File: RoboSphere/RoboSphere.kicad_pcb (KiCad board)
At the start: 2 copper layers, 2 parts, among them U1 RASPBERRY_PI_ZERO_2_W, U4 DRV8833PW

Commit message: Kicad H-bridge update
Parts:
- added C1: 0.01uF, Capacitor_SMD:C_0805_2012Metric, F.Cu at (41.0, 56.3)
- added C2: 10uF, Capacitor_SMD:C_0805_2012Metric, F.Cu at (41.0, 59.3)
- added C3: 2.2uF, Capacitor_SMD:C_0805_2012Metric, F.Cu at (41.0, 62.3)
- added J2: Conn_01x04_Pin, Connector_PinHeader_2.54mm:PinHeader_1x04_P2.54mm_Vertical, F.Cu at (27.3, 57.1)
- moved U1 4.97 mm to (60.0, 38.5)
- moved U4 2.36 mm to (34.4, 58.1)
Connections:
- U4 pad 10: Net-(U4-BIN2) -> Net-(U1-GPIO2/SDA1)
- U4 pad 12: Net-(U4-VM) -> +10V
- U4 pad 13: Net-(U4-GND) -> GND
- U4 pad 14: unconnected-(U4-VINT-Pad14) -> Net-(U4-VINT)
- U4 pad 15: Net-(U4-AIN2) -> Net-(U1-GPIO4/GPIO_GCLK)
- U4 pad 16: Net-(U4-AIN1) -> Net-(U1-GPIO5)
- U4 pad 2: Net-(M4-+) -> /AOUT1
- U4 pad 4: Net-(M4--) -> /AOUT2
- U4 pad 5: Net-(M1-+) -> /BOUT2
- U4 pad 7: Net-(M1--) -> /BOUT1
- U4 pad 9: Net-(U4-BIN1) -> Net-(U1-GPIO3/SCL)

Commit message: Power Converter Module
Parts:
- removed J2: Conn_01x04_Pin, Connector_PinHeader_2.54mm:PinHeader_1x04_P2.54mm_Vertical
- removed U4: DRV8833PW, Package_SO:TSSOP-16_4.4x5mm_P0.65mm
- added 3350mAh1: 3.6V, Battery:BatteryHolder_Keystone_1042_1x18650, F.Cu at (67.6, 101.0)
- added 3350mAh2: 3.6V, Battery:BatteryHolder_Keystone_1042_1x18650, F.Cu at (67.6, 78.3)
- added AOUT1: Conn_01x03_Pin, Connector_PinHeader_2.54mm:PinHeader_1x03_P2.54mm_Vertical_SMD_Pin1Left, F.Cu at (44.3, 44.5)
- added AOUT2: Conn_01x03_Pin, Connector_PinHeader_2.54mm:PinHeader_1x03_P2.54mm_Vertical_SMD_Pin1Left, F.Cu at (29.8, 44.5)
- added BOUT1: Conn_01x03_Pin, Connector_PinHeader_2.54mm:PinHeader_1x03_P2.54mm_Vertical_SMD_Pin1Left, F.Cu at (44.3, 56.5)
- added BOUT2: Conn_01x03_Pin, Connector_PinHeader_2.54mm:PinHeader_1x03_P2.54mm_Vertical_SMD_Pin1Left, F.Cu at (29.8, 56.5)
- added U2: DRV8833PWP, Package_SO:HTSSOP-16-1EP_4.4x5mm_P0.65mm_EP3.4x5mm_Mask2.46x2.31mm_ThermalVias, F.Cu at (55.4, 50.5)
- moved U1 74.6 mm to (134.5, 35.0)
- moved C3 28.3 mm to (64.3, 46.3)
- moved C2 25.9 mm to (65.2, 50.2), turned to 90 degrees
- moved C1 23.3 mm to (64.2, 54.3), turned to 180 degrees
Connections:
- net +10V renamed +6V
- U1 pad 33: unconnected-(U1-GPIO13-Pad33) -> Net-(U1-GPIO13)
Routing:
- net GND: track 0.00 -> 60.6 mm
- net /AOUT2: track 0.00 -> 39.2 mm
- net /BOUT2: track 0.00 -> 38.8 mm
- net /AOUT1: track 0.00 -> 24.1 mm
- net /BOUT1: track 0.00 -> 23.8 mm
- net +6V: track 0.00 -> 10.3 mm
- net Net-(U2-VINT): track 0.00 -> 6.45 mm
- net Net-(U2-VCP): track 0.00 -> 6.16 mm
- net +5V: track 0.00 -> 2.54 mm

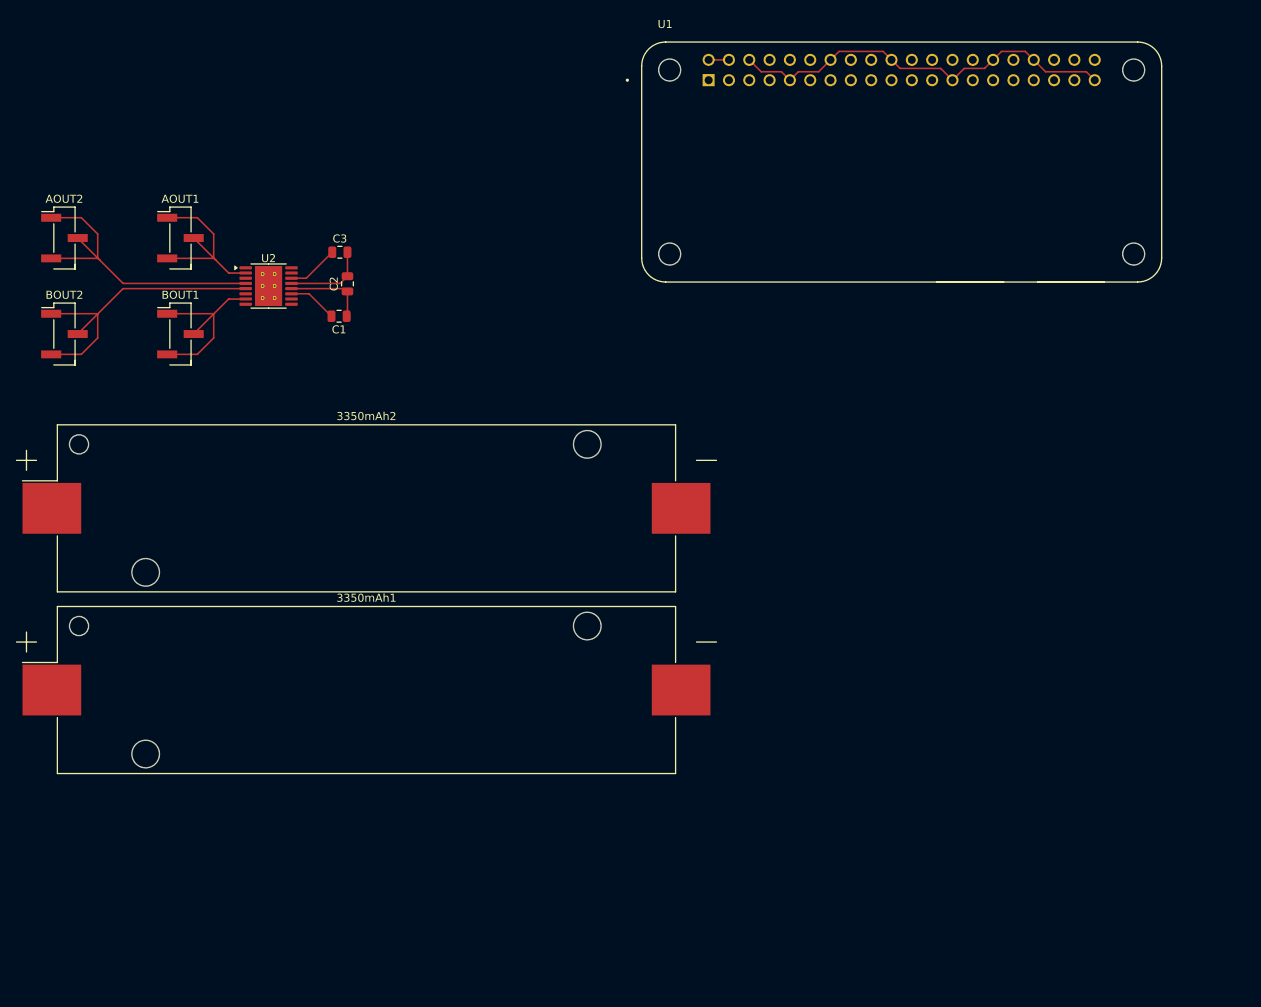
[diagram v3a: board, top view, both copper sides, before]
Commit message: Updated schematic with placement organization
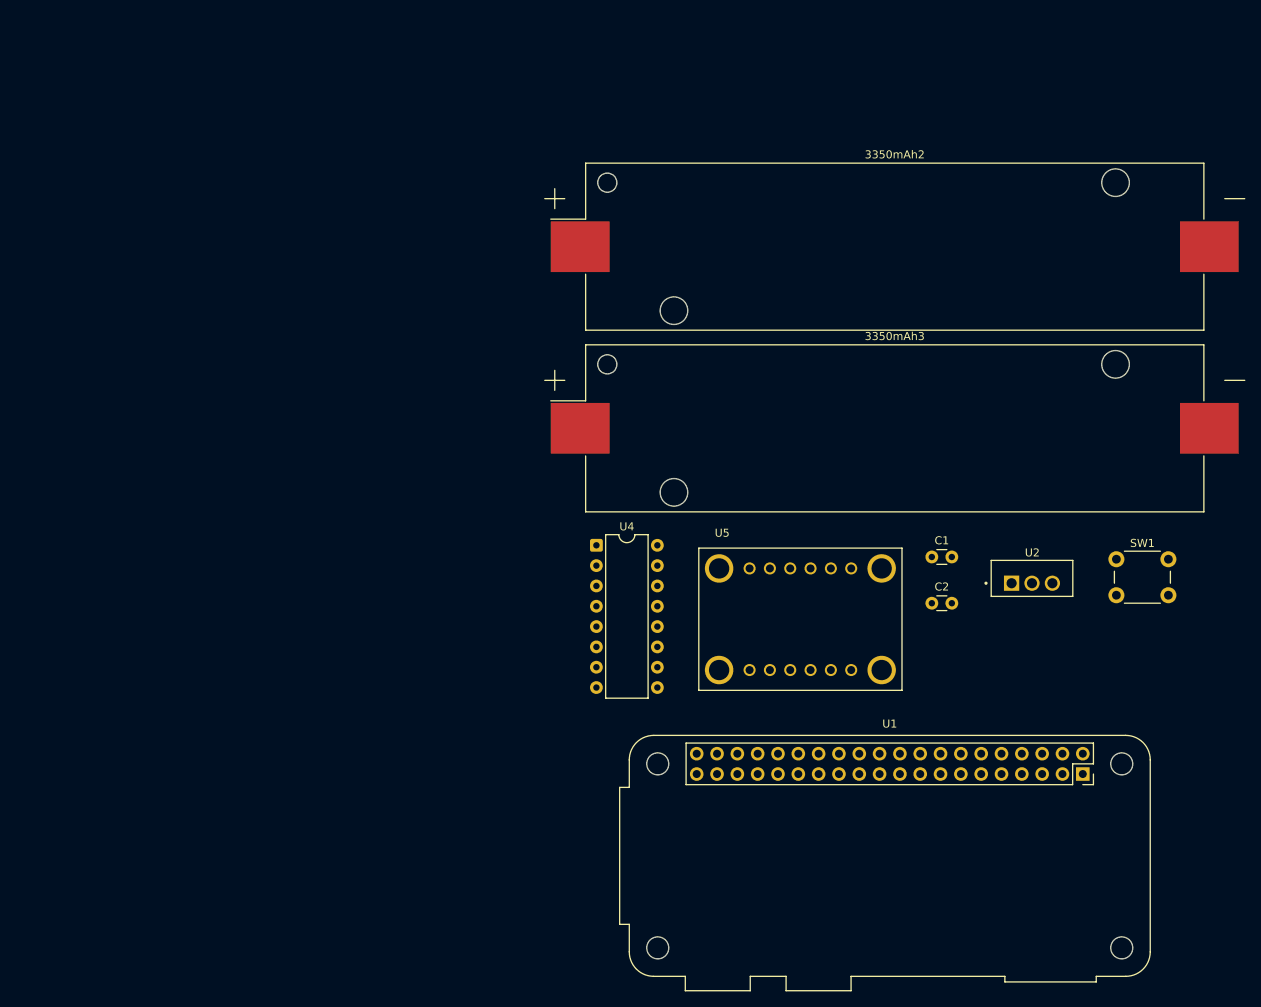
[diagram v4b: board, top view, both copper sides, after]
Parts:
- removed 3350mAh1: 3.6V, Battery:BatteryHolder_Keystone_1042_1x18650
- removed AOUT1, AOUT2, BOUT1, BOUT2: Conn_01x03_Pin, Connector_PinHeader_2.54mm:PinHeader_1x03_P2.54mm_Vertical_SMD_Pin1Left
- removed C3: 2.2uF, Capacitor_SMD:C_0805_2012Metric
- added 3350mAh3: 3.7V, Battery:BatteryHolder_Keystone_1042_1x18650, F.Cu at (133.6, 68.3)
- added SW1: SW_Push, Button_Switch_THT:SW_PUSH_6mm, F.Cu at (161.3, 84.7)
- added U4: L293D, Package_DIP:DIP-16_W7.62mm, F.Cu at (96.3, 82.9)
- added U5: ADS1115 1085, 1085:MODULE_1085, F.Cu at (121.8, 92.2)
- 3350mAh2: value 3.6V -> 3.7V
- C1: value 0.01uF -> C; footprint Capacitor_SMD:C_0805_2012Metric -> Capacitor_THT:C_Disc_D3.0mm_W1.6mm_P2.50mm
- C2: value 10uF -> C; footprint Capacitor_SMD:C_0805_2012Metric -> Capacitor_THT:C_Disc_D3.0mm_W1.6mm_P2.50mm
- U1: footprint RASPBERRY_PI_ZERO_2_W:MODULE_RASPBERRY_PI_ZERO_2_W -> Module:Raspberry_Pi_Zero_Socketed_THT_FaceDown_MountingHoles
- U2: value DRV8833PWP -> L7806; footprint Package_SO:HTSSOP-16-1EP_4.4x5mm_P0.65mm_EP3.4x5mm_Mask2.46x2.31mm_ThermalVias -> L7806CV:TO255P1020X450X1968-3B
- moved U2 102.4 mm to (150.8, 87.7)
- moved C2 83.2 mm to (138.3, 90.2), turned to 0 degrees
- moved C1 80.0 mm to (138.3, 84.4), turned to 0 degrees
- moved U1 79.8 mm to (157.1, 111.5), turned to -90 degrees
- moved 3350mAh2 73.7 mm to (133.6, 45.6)
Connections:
- 3350mAh2 pad 1: unconnected-(3350mAh2-+-Pad1) -> Net-(3350mAh2-+)
- 3350mAh2 pad 2: unconnected-(3350mAh2---Pad2) -> GND
- C1 pad 1: +6V -> GND
- C1 pad 2: Net-(U2-VCP) -> +7.5V
- C2 pad 1: +6V -> GND
- C2 pad 2: GND -> +6V
- U1 pad 1: unconnected-(U1-3V3_1-Pad1) -> Net-(U1-3V3_1)
- U1 pad 14: GND -> unconnected-(U1-GND_14-Pad14)
- U1 pad 16: unconnected-(U1-GPIO23/GPIO_GEN4-Pad16) -> Net-(U1-GPIO23/GPIO_GEN4)
- U1 pad 18: unconnected-(U1-GPIO24/GPIO_GEN5-Pad18) -> Net-(U1-GPIO24/GPIO_GEN5)
- U1 pad 2: +5V -> unconnected-(U1-5V_2-Pad2)
- U1 pad 20: GND -> unconnected-(U1-GND_20-Pad20)
- U1 pad 24: unconnected-(U1-GPIO8/SPI_~{CE0}-Pad24) -> Net-(U1-GPIO8/SPI_~{CE0})
- U1 pad 25: GND -> unconnected-(U1-GND_25-Pad25)
- U1 pad 26: unconnected-(U1-GPIO7/SPI_~{CE1}-Pad26) -> Net-(U1-GPIO7/SPI_~{CE1})
- U1 pad 30: GND -> unconnected-(U1-GND_30-Pad30)
- U1 pad 34: GND -> unconnected-(U1-GND_34-Pad34)
- U1 pad 35: unconnected-(U1-GPIO19-Pad35) -> Net-(U1-GPIO19)
- U1 pad 39: GND -> unconnected-(U1-GND_39-Pad39)
- U1 pad 4: +5V -> unconnected-(U1-5V_4-Pad4)
- U1 pad 6: GND -> unconnected-(U1-GND_6-Pad6)
- U1 pad 7: Net-(U1-GPIO4/GPIO_GCLK) -> unconnected-(U1-GPIO4/GPIO_GCLK-Pad7)
- U1 pad 8: Net-(U1-GPIO14/TXD0) -> unconnected-(U1-GPIO14/TXD0-Pad8)
- U1 pad 9: GND -> unconnected-(U1-GND_9-Pad9)
- U2 pad 1: Net-(U1-GPIO13) -> +7.5V
- U2 pad 2: /AOUT1 -> GND
- U2 pad 3: GND -> +6V
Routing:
- net GND: track 60.6 -> 0.00 mm
- net /AOUT2: track 39.2 -> 0.00 mm
- net /BOUT2: track 38.8 -> 0.00 mm
- net /AOUT1: track 24.1 -> 0.00 mm
- net /BOUT1: track 23.8 -> 0.00 mm
- net +6V: track 10.3 -> 0.00 mm
- net Net-(U2-VINT): track 6.45 -> 0.00 mm
- net Net-(U2-VCP): track 6.16 -> 0.00 mm
- net +5V: track 2.54 -> 0.00 mm
